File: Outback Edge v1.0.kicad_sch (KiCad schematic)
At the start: 19 parts, among them J1 USB_C_Receptacle_USB2.0_16P, J2 OE_M.2_Socket_E, J3 RJ45_LED_Shielded, J4 Micro_SD_Card_Det_Hirose_DM3AT, J5 USB3_A_Stacked, SW1 SW_Push, U1 R7FA6M5AH3CFB#AA0, U2 USB2514B_Bi

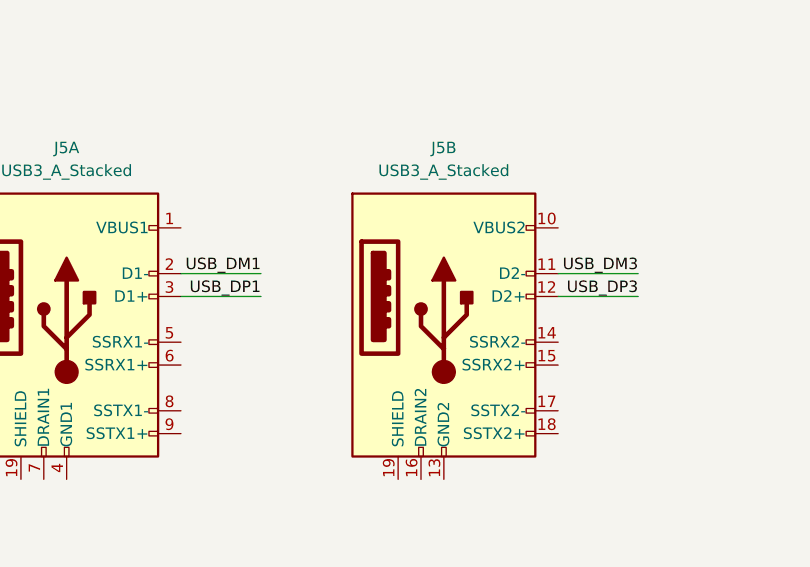
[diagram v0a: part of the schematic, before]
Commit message: Clarify USB2-only SuperSpeed handling
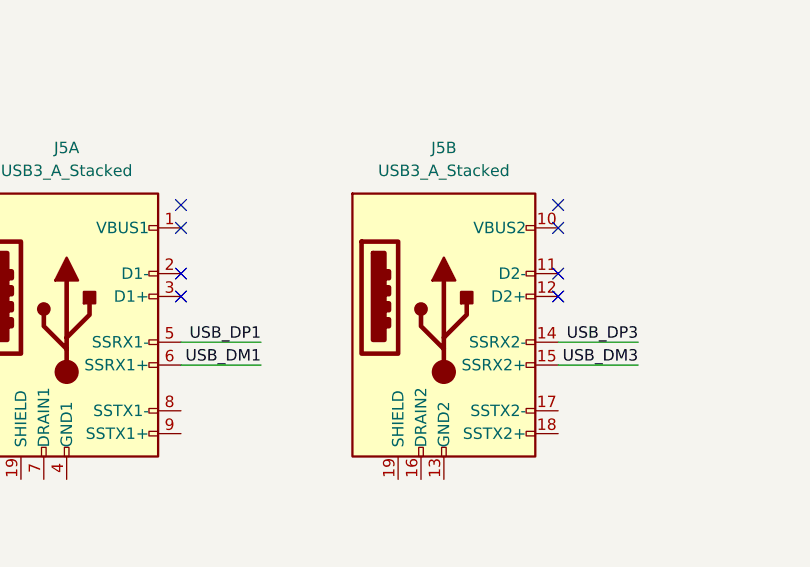
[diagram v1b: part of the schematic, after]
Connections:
- net USB_DM1: now also J5.6 (SSRX1+); no longer J5.2 (D1-)
- net USB_DM3: now also J5.15 (SSRX2+); no longer J5.11 (D2-)
- net USB_DP1: now also J5.5 (SSRX1-); no longer J5.3 (D1+)
- net USB_DP3: now also J5.14 (SSRX2-); no longer J5.12 (D2+)
- no-connect marks 0 -> 8
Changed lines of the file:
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@@
 	(wire
 		(pts
-			(xy 162.56 46.99) (xy 153.67 46.99)
+			(xy 162.56 57.15) (xy 153.67 57.15)
 		)
 		(stroke
@@
 	(wire
 		(pts
-			(xy 162.56 49.53) (xy 153.67 49.53)
+			(xy 162.56 54.61) (xy 153.67 54.61)
 		)
 		(stroke
@@
 	(wire
 		(pts
-			(xy 120.65 49.53) (xy 111.76 49.53)
+			(xy 120.65 54.61) (xy 111.76 54.61)
 		)
 		(stroke
@@
 	(wire
 		(pts
-			(xy 120.65 46.99) (xy 111.76 46.99)
+			(xy 120.65 57.15) (xy 111.76 57.15)
 		)
 		(stroke
@@
 	)
 	(label "USB_DM3"
-		(at 162.56 46.99 180)
+		(at 162.56 57.15 180)
 		(effects
 			(font
@@
 	)
 	(label "USB_DP1"
-		(at 120.65 49.53 180)
+		(at 120.65 54.61 180)
 		(effects
 			(font
@@
 	)
 	(label "USB_DP3"
-		(at 162.56 49.53 180)
+		(at 162.56 54.61 180)
 		(effects
 			(font
@@
 	)
 	(label "USB_DM1"
-		(at 120.65 46.99 180)
+		(at 120.65 57.15 180)
 		(effects
 			(font
@@
 		)
 	)
+	(no_connect
+		(at 111.76 49.53)
+	)
+	(no_connect
+		(at 111.76 46.99)
+	)
+	(no_connect
+		(at 111.76 41.91)
+	)
+	(no_connect
+		(at 111.76 39.37)
+	)
+	(no_connect
+		(at 153.67 49.53)
+	)
+	(no_connect
+		(at 153.67 46.99)
+	)
+	(no_connect
+		(at 153.67 41.91)
+	)
+	(no_connect
+		(at 153.67 39.37)
+	)
 	(sheet_instances
